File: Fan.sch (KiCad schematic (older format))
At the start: 0 parts

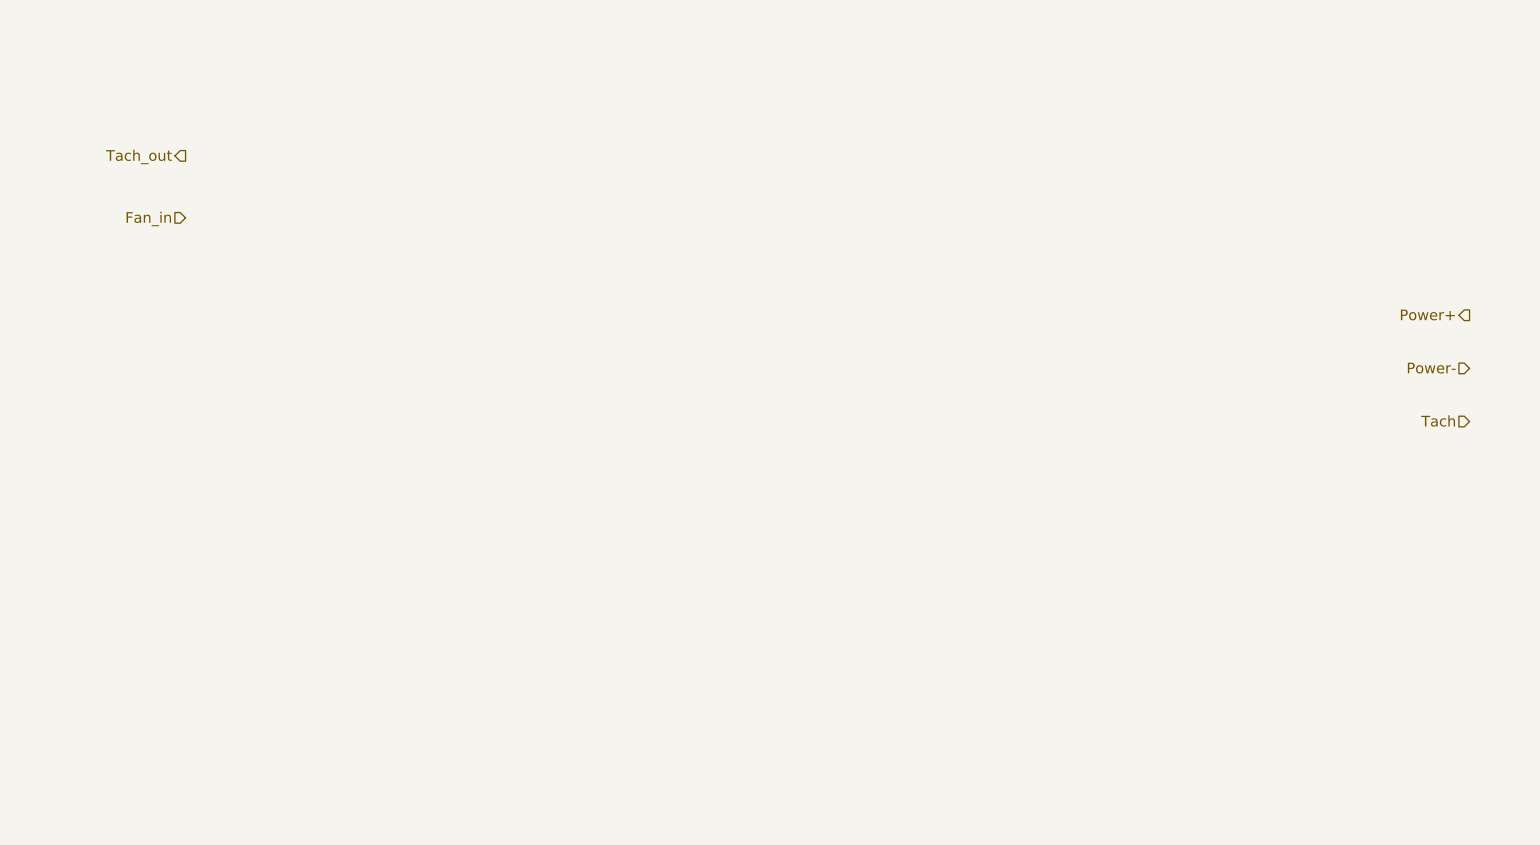
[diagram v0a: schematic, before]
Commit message: After Current/Fan Driver Module
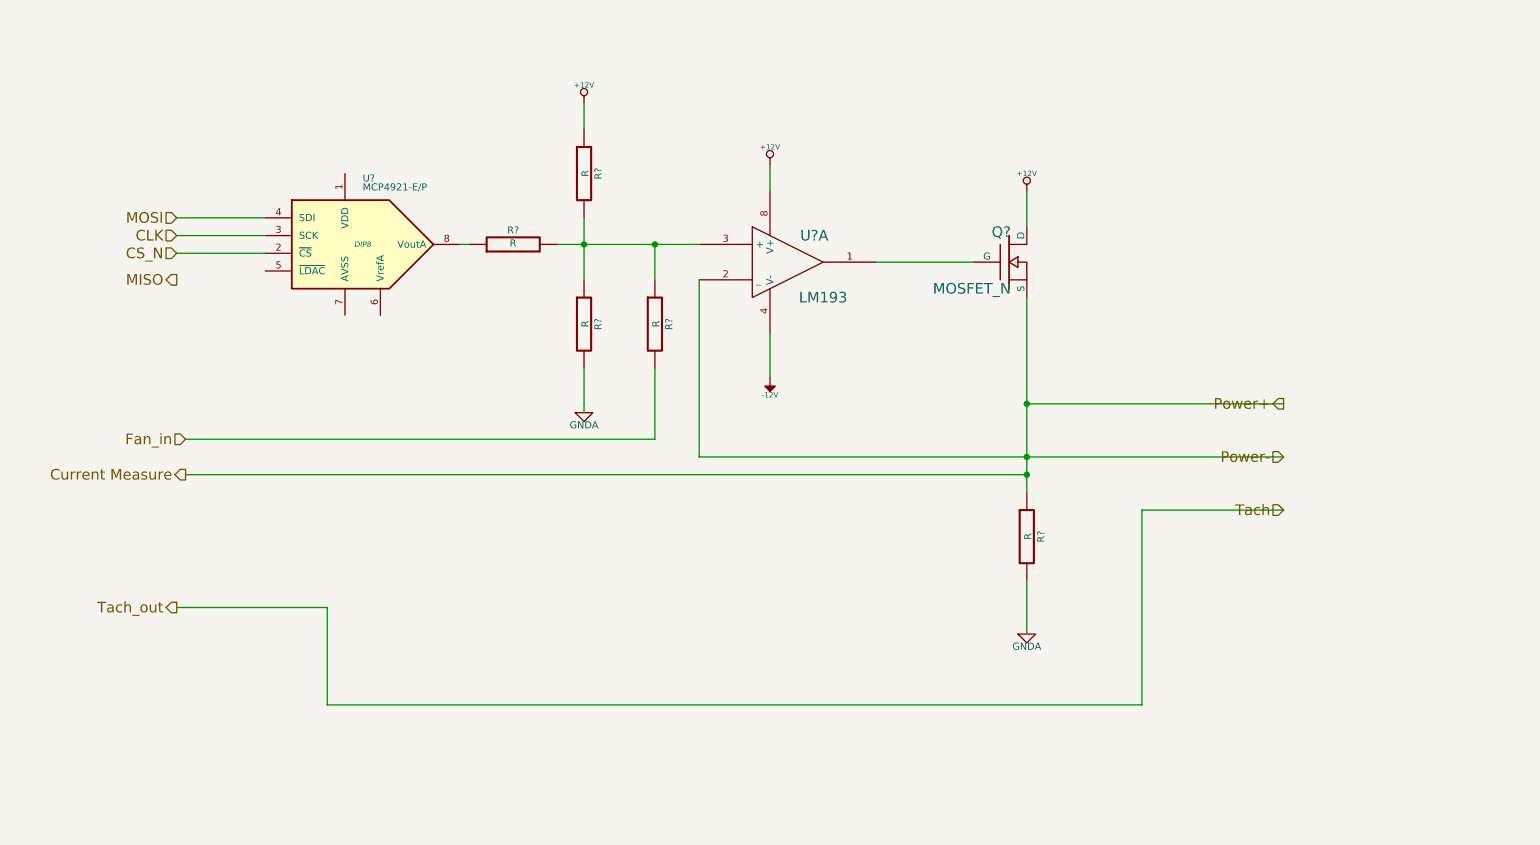
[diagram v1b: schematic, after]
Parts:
- added Q?: MOSFET_N, ~, symbol MOSFET_N
- added R? (x5): R, ~, symbol R
- added U?: LM193, symbol LM193
- added U?: MCP4921-E/P, DIP8, symbol MCP4921-E/P
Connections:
- net Fan_in: now also R?.2
- new net: Q?.G, U?.1
- new net: R?.1, R?.1, R?.2, R?.2, U?.3 (+)
- new net: R?.1, U?.8 (VoutA)
- new net +12V: Q?.D, R?.1, U?.8 (V+)
- new net -12V: U?.4 (V-)
- new net CLK: U?.3 (SCK)
- new net CS_N: U?.2 (~CS~)
- new net Current Measure: Q?.S, R?.1, U?.2 (_)
- new net GNDA: R?.2, R?.2
- new net MOSI: U?.4 (SDI)
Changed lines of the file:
@@
 $Descr A4 11693 8268
 encoding utf-8
-Sheet 7 8
+Sheet 8 8
 Title ""
 Date "4 feb 2014"
@@
 Comment4 ""
 $EndDescr
-Text HLabel 8650 2350 0    60   Output ~ 0
+Text HLabel 7600 2850 0    60   Output ~ 0
 Power+
-Text HLabel 8650 2650 0    60   Input ~ 0
+Text HLabel 7600 3150 0    60   Input ~ 0
 Power-
-Text HLabel 8650 2950 0    60   Input ~ 0
+Text HLabel 7600 3450 0    60   Input ~ 0
 Tach
-Text HLabel 1400 1450 0    60   Output ~ 0
+Text HLabel 1350 4000 0    60   Output ~ 0
 Tach_out
-Text HLabel 1400 1800 0    60   Input ~ 0
+Text HLabel 1400 3050 0    60   Input ~ 0
 Fan_in
+$Comp
+L LM193 U?
+U 1 1 52F14C74
+P 4800 2050
+F 0 "U?" H 4950 2200 60  0000 C CNN
+F 1 "LM193" H 5000 1850 60  0000 C CNN
+F 2 "" H 4800 2050 60  0000 C CNN
+F 3 "" H 4800 2050 60  0000 C CNN
+	1    4800 2050
+	1    0    0    -1
+$EndComp
+$Comp
+L MOSFET_N Q?
+U 1 1 52F14CD9
+P 6050 2050
+F 0 "Q?" H 6060 2220 60  0000 R CNN
+F 1 "MOSFET_N" H 6060 1900 60  0000 R CNN
+F 2 "~" H 6050 2050 60  0000 C CNN
+F 3 "~" H 6050 2050 60  0000 C CNN
+	1    6050 2050
+	1    0    0    -1
+$EndComp
+$Comp
+L +12V #PWR?
+U 1 1 52F14CF5
+P 6150 1650
+F 0 "#PWR?" H 6150 1600 20  0001 C CNN
+F 1 "+12V" H 6150 1750 30  0000 C CNN
+F 2 "" H 6150 1650 60  0000 C CNN
+F 3 "" H 6150 1650 60  0000 C CNN
+	1    6150 1650
+	1    0    0    -1
+$EndComp
+Wire Wire Line
+	5300 2050 5850 2050
+Wire Wire Line
+	6150 2250 6150 3350
+Wire Wire Line
+	6150 2850 7600 2850
+$Comp
+L R R?
+U 1 1 52F14DA9
+P 6150 3600
+F 0 "R?" V 6230 3600 40  0000 C CNN
+F 1 "R" V 6157 3601 40  0000 C CNN
+F 2 "~" V 6080 3600 30  0000 C CNN
+F 3 "~" H 6150 3600 30  0000 C CNN
+	1    6150 3600
+	1    0    0    -1
+$EndComp
+Connection ~ 6150 2850
+$Comp
+L GNDA #PWR?
+U 1 1 52F14DE1
+P 6150 4150
+F 0 "#PWR?" H 6150 4150 40  0001 C CNN
+F 1 "GNDA" H 6150 4080 40  0000 C CNN
+F 2 "" H 6150 4150 60  0000 C CNN
+F 3 "" H 6150 4150 60  0000 C CNN
+	1    6150 4150
+	1    0    0    -1
+$EndComp
+Wire Wire Line
+	6150 4150 6150 3850
+Wire Wire Line
+	4300 3150 7600 3150
+Connection ~ 6150 3150
+Wire Wire Line
+	4300 3150 4300 2150
+Wire Wire Line
+	6150 1850 6150 1650
+$Comp
+L +12V #PWR?
+U 1 1 52F14E59
+P 4700 1500
+F 0 "#PWR?" H 4700 1450 20  0001 C CNN
+F 1 "+12V" H 4700 1600 30  0000 C CNN
+F 2 "" H 4700 1500 60  0000 C CNN
+F 3 "" H 4700 1500 60  0000 C CNN
+	1    4700 1500
+	1    0    0    -1
+$EndComp
+Wire Wire Line
+	4700 1500 4700 1650
+$Comp
+L -12V #PWR?
+U 1 1 52F14EBF
+P 4700 2700
+F 0 "#PWR?" H 4700 2830 20  0001 C CNN
+F 1 "-12V" H 4700 2800 30  0000 C CNN
+F 2 "" H 4700 2700 60  0000 C CNN
+F 3 "" H 4700 2700 60  0000 C CNN
+	1    4700 2700
+	-1   0    0    1
+$EndComp
+Wire Wire Line
+	4700 2450 4700 2700
+$Comp
+L R R?
+U 1 1 52F14F89
+P 3650 1550
+F 0 "R?" V 3730 1550 40  0000 C CNN
+F 1 "R" V 3657 1551 40  0000 C CNN
+F 2 "~" V 3580 1550 30  0000 C CNN
+F 3 "~" H 3650 1550 30  0000 C CNN
+	1    3650 1550
+	1    0    0    -1
+$EndComp
+$Comp
+L R R?
+U 1 1 52F14F93
+P 3650 2400
+F 0 "R?" V 3730 2400 40  0000 C CNN
+F 1 "R" V 3657 2401 40  0000 C CNN
+F 2 "~" V 3580 2400 30  0000 C CNN
+F 3 "~" H 3650 2400 30  0000 C CNN
+	1    3650 2400
+	1    0    0    -1
+$EndComp
+$Comp
+L +12V #PWR?
+U 1 1 52F14FA2
+P 3650 1150
+F 0 "#PWR?" H 3650 1100 20  0001 C CNN
+F 1 "+12V" H 3650 1250 30  0000 C CNN
+F 2 "" H 3650 1150 60  0000 C CNN
+F 3 "" H 3650 1150 60  0000 C CNN
+	1    3650 1150
+	1    0    0    -1
+$EndComp
+Wire Wire Line
+	3650 1150 3650 1300
+Wire Wire Line
+	3650 1800 3650 2150
+Wire Wire Line
+	3500 1950 4300 1950
+Connection ~ 3650 1950
+$Comp
+L GNDA #PWR?
+U 1 1 52F14FD1
+P 3650 2900
+F 0 "#PWR?" H 3650 2900 40  0001 C CNN
+F 1 "GNDA" H 3650 2830 40  0000 C CNN
+F 2 "" H 3650 2900 60  0000 C CNN
+F 3 "" H 3650 2900 60  0000 C CNN
+	1    3650 2900
+	1    0    0    -1
+$EndComp
+Wire Wire Line
+	3650 2650 3650 2900
+$Comp
+L MCP4921-E/P U?
+U 1 1 52F1512C
+P 2400 1950
+F 0 "U?" H 2400 2300 40  0000 L BNN
+F 1 "MCP4921-E/P" H 2400 2250 40  0000 L BNN
+F 2 "DIP8" H 2400 1950 30  0000 C CIN
+F 3 "" H 2400 1950 60  0000 C CNN
+	1    2400 1950
+	1    0    0    -1
+$EndComp
+Wire Wire Line
+	7600 3450 6800 3450
+Wire Wire Line
+	6800 3450 6800 4550
+Wire Wire Line
+	6800 4550 2200 4550
+Wire Wire Line
+	2200 4550 2200 4000
+Wire Wire Line
+	2200 4000 1350 4000
+Text HLabel 1400 3250 0    60   Output ~ 0
+Current Measure
+Wire Wire Line
+	6150 3250 1400 3250
+Connection ~ 6150 3250
+$Comp
+L R R?
+U 1 1 52F15EEC
+P 4050 2400
+F 0 "R?" V 4130 2400 40  0000 C CNN
+F 1 "R" V 4057 2401 40  0000 C CNN
+F 2 "~" V 3980 2400 30  0000 C CNN
+F 3 "~" H 4050 2400 30  0000 C CNN
+	1    4050 2400
+	1    0    0    -1
+$EndComp
+Wire Wire Line
+	4050 2150 4050 1950
+Connection ~ 4050 1950
+Wire Wire Line
+	4050 2650 4050 3050
+Wire Wire Line
+	4050 3050 1400 3050
+$Comp
+L R R?
+U 1 1 52F15F30
+P 3250 1950
+F 0 "R?" V 3330 1950 40  0000 C CNN
+F 1 "R" V 3257 1951 40  0000 C CNN
+F 2 "~" V 3180 1950 30  0000 C CNN
+F 3 "~" H 3250 1950 30  0000 C CNN
+	1    3250 1950
+	0    -1   -1   0
+$EndComp
+Wire Wire Line
+	3000 1950 2950 1950
+Text HLabel 1350 1800 0    60   Input ~ 0
+MOSI
+Text HLabel 1350 2150 0    60   Output ~ 0
+MISO
+Text HLabel 1350 1900 0    60   Input ~ 0
+CLK
+Text HLabel 1350 2000 0    60   Input ~ 0
+CS_N
+Wire Wire Line
+	1850 1800 1350 1800
+Wire Wire Line
+	1350 1900 1850 1900
+Wire Wire Line
+	1350 2000 1850 2000
 $EndSCHEMATC

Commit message: Finished Week 3, Unit 10: Revisiting The Current Fan Module
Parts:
- removed R? (x3): R, ~, symbol R
- removed U?: MCP4921-E/P, DIP8, symbol MCP4921-E/P
- added D?: DIODE, ~, symbol DIODE
- added Q? (x2): MOSFET_N, ~, symbol MOSFET_N
- added TH?: THERMISTOR, ~, symbol THERMISTOR
- added U?: MCP4922-E/P, DIP14, symbol MCP4922-E/P
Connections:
- net +12V: no longer Q?.D
- net CLK: now also U?.4 (SCK)
- net CS_N: now also U?.3 (~CS~)
- net GNDA: now also Q?.S
- net MOSI: now also U?.5 (SDI)
- net at R?.2, U?.3 (+): now also Q?.D
- net at R?.1: now also U?.14 (VoutA)
- net Current Measure renamed CURR_MEAS
- net CURR_MEAS: now also Q?.D; no longer U?.2 (_)
- new net +12C: TH?.1
- new net AGND: Q?.S
- new net FAN_MODE: Q?.G
- new net FAN_OUT+: D?.2 (K), TH?.2
- new net FAN_OUT-: D?.1 (A), Q?.D
- new net FAN_PWM: Q?.G
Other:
- moved on the sheet: Q?, R?, U?A
